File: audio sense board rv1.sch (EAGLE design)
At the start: 33 parts, among them IC2 TSOP38238, J1 PJRAN1X1U01X, J2 PJRAN1X1U01X, Q1 2N3904, Q2 2N3904

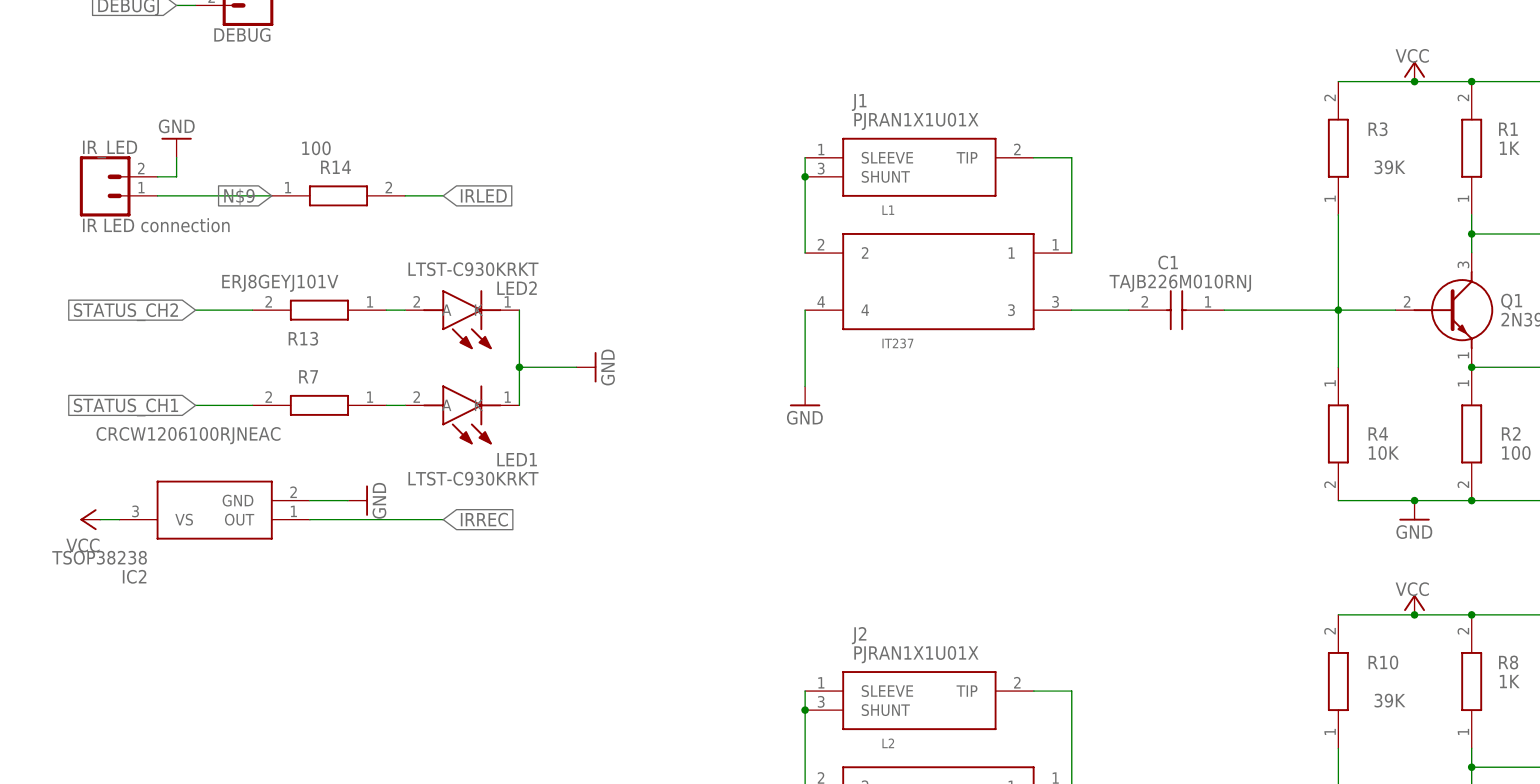
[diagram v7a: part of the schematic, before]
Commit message: update component values on output LEDs
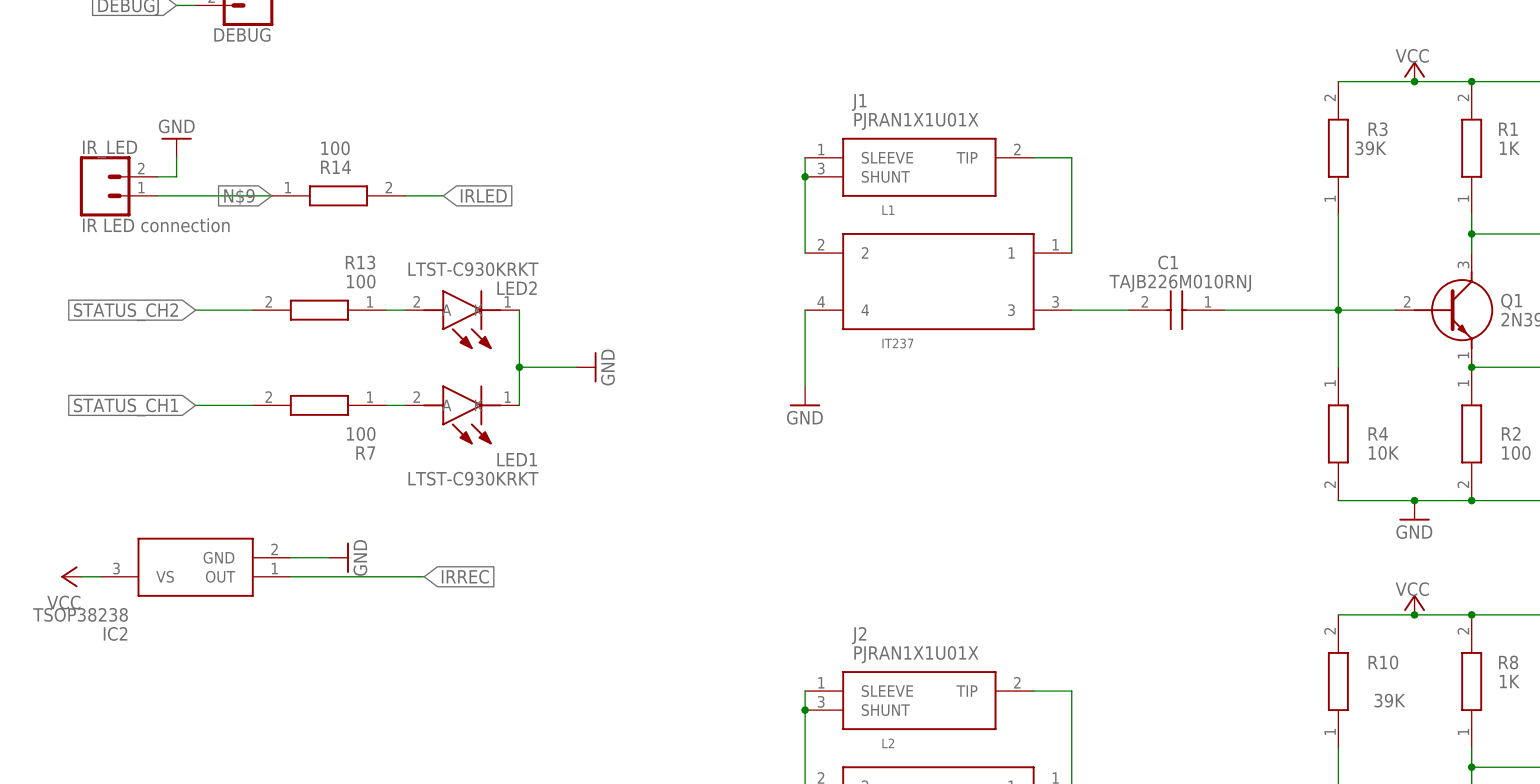
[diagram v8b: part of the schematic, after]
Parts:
- R13: value ERJ8GEYJ101V -> 100
- R7: value CRCW1206100RJNEAC -> 100; device Samac Populated:CRCW1206100RJNEAC -> Samac Populated:ERJ8GEYJ101V
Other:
- moved on the sheet: IC2
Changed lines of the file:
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@@
 <part name="LED1" library="Samac Populated" deviceset="LTST-C930KRKT" device=""/>
 <part name="LED2" library="Samac Populated" deviceset="LTST-C930KRKT" device=""/>
-<part name="R7" library="Samac Populated" deviceset="CRCW1206100RJNEAC" device=""/>
-<part name="R13" library="Samac Populated" deviceset="ERJ8GEYJ101V" device=""/>
+<part name="R7" library="Samac Populated" deviceset="ERJ8GEYJ101V" device="" value="100"/>
+<part name="R13" library="Samac Populated" deviceset="ERJ8GEYJ101V" device="" value="100"/>
 <part name="GND4" library="supply1" library_urn="urn:adsk.eagle:library:371" deviceset="GND" device=""/>
 <part name="R14" library="Samac Populated" deviceset="CRCW1206100RJNEAC" device="" value="100"/>
@@
 <attribute name="VALUE" x="-17.78" y="137.16" size="1.778" layer="96" rot="R90"/>
 </instance>
-<instance part="IC2" gate="G$1" x="-137.16" y="30.48" smashed="yes" rot="R180">
-<attribute name="NAME" x="-158.75" y="22.86" size="1.778" layer="95" rot="R180" align="center-left"/>
-<attribute name="VALUE" x="-158.75" y="25.4" size="1.778" layer="96" rot="R180" align="center-left"/>
+<instance part="IC2" gate="G$1" x="-139.7" y="22.86" smashed="yes" rot="R180">
+<attribute name="NAME" x="-161.29" y="15.24" size="1.778" layer="95" rot="R180" align="center-left"/>
+<attribute name="VALUE" x="-161.29" y="17.78" size="1.778" layer="96" rot="R180" align="center-left"/>
 </instance>
 <instance part="GND5" gate="1" x="-154.94" y="81.28" smashed="yes" rot="R180">
@@
 <attribute name="NAME" x="-167.64" y="79.248" size="1.778" layer="95" font="vector"/>
 </instance>
-<instance part="GND6" gate="1" x="-129.54" y="33.02" smashed="yes" rot="R90">
-<attribute name="VALUE" x="-127" y="30.48" size="1.778" layer="96" rot="R90"/>
+<instance part="GND6" gate="1" x="-132.08" y="25.4" smashed="yes" rot="R90">
+<attribute name="VALUE" x="-129.54" y="22.86" size="1.778" layer="96" rot="R90"/>
 </instance>
 <instance part="P+1" gate="VCC" x="-25.4" y="134.62" smashed="yes" rot="R270">
 <attribute name="VALUE" x="-27.94" y="137.16" size="1.778" layer="96"/>
 </instance>
-<instance part="P+2" gate="VCC" x="-167.64" y="30.48" smashed="yes" rot="R90">
-<attribute name="VALUE" x="-165.1" y="27.94" size="1.778" layer="96" rot="R180"/>
+<instance part="P+2" gate="VCC" x="-170.18" y="22.86" smashed="yes" rot="R90">
+<attribute name="VALUE" x="-167.64" y="20.32" size="1.778" layer="96" rot="R180"/>
 </instance>
 <instance part="GND7" gate="1" x="-73.66" y="134.62" smashed="yes" rot="R270">
@@
 </instance>
 <instance part="R7" gate="G$1" x="-127" y="45.72" smashed="yes" rot="R180">
-<attribute name="NAME" x="-135.89" y="49.53" size="1.778" layer="95" rot="R180" align="center-left"/>
-<attribute name="VALUE" x="-140.97" y="41.91" size="1.778" layer="96" rot="R180" align="center-left"/>
+<attribute name="NAME" x="-128.27" y="39.37" size="1.778" layer="95" rot="R180" align="center-left"/>
+<attribute name="VALUE" x="-128.27" y="41.91" size="1.778" layer="96" rot="R180" align="center-left"/>
 </instance>
 <instance part="R13" gate="G$1" x="-127" y="58.42" smashed="yes" rot="R180">
-<attribute name="NAME" x="-135.89" y="54.61" size="1.778" layer="95" rot="R180" align="center-left"/>
-<attribute name="VALUE" x="-133.35" y="62.23" size="1.778" layer="96" rot="R180" align="center-left"/>
+<attribute name="NAME" x="-128.27" y="64.77" size="1.778" layer="95" rot="R180" align="center-left"/>
+<attribute name="VALUE" x="-128.27" y="62.23" size="1.778" layer="96" rot="R180" align="center-left"/>
 </instance>
 <instance part="GND4" gate="1" x="-99.06" y="50.8" smashed="yes" rot="R90">
@@
 <instance part="R14" gate="G$1" x="-142.24" y="73.66" smashed="yes">
 <attribute name="NAME" x="-135.89" y="77.47" size="1.778" layer="95" align="center-left"/>
-<attribute name="VALUE" x="-138.43" y="80.01" size="1.778" layer="96" align="center-left"/>
+<attribute name="VALUE" x="-135.89" y="80.01" size="1.778" layer="96" align="center-left"/>
 </instance>
 <instance part="J1" gate="G$1" x="-71.12" y="78.74" smashed="yes">
@@
 <instance part="R3" gate="G$1" x="0" y="71.12" smashed="yes" rot="R90">
 <attribute name="NAME" x="3.81" y="82.55" size="1.778" layer="95" align="center-left"/>
-<attribute name="VALUE" x="8.89" y="77.47" size="1.778" layer="96" rot="R180" align="center-left"/>
+<attribute name="VALUE" x="6.35" y="80.01" size="1.778" layer="96" rot="R180" align="center-left"/>
 </instance>
 <instance part="R4" gate="G$1" x="0" y="50.8" smashed="yes" rot="R270">
@@
 <pinref part="GND6" gate="1" pin="GND"/>
 <pinref part="IC2" gate="G$1" pin="GND"/>
-<wire x1="-132.08" y1="33.02" x2="-137.16" y2="33.02" width="0.1524" layer="91"/>
+<wire x1="-134.62" y1="25.4" x2="-139.7" y2="25.4" width="0.1524" layer="91"/>
 </segment>
 <segment>
@@
 <pinref part="P+2" gate="VCC" pin="VCC"/>
 <pinref part="IC2" gate="G$1" pin="VS"/>
-<wire x1="-162.56" y1="30.48" x2="-165.1" y2="30.48" width="0.1524" layer="91"/>
+<wire x1="-165.1" y1="22.86" x2="-167.64" y2="22.86" width="0.1524" layer="91"/>
 </segment>
 <segment>
@@
 <segment>
 <pinref part="IC2" gate="G$1" pin="OUT"/>
-<wire x1="-137.16" y1="30.48" x2="-119.38" y2="30.48" width="0.1524" layer="91"/>
-<label x="-119.38" y="30.48" size="1.778" layer="95" xref="yes"/>
-</segment>
-<segment>
+<wire x1="-139.7" y1="22.86" x2="-121.92" y2="22.86" width="0.1524" layer="91"/>
+<label x="-121.92" y="22.86" size="1.778" layer="95" xref="yes"/>
+</segment>
+<segment>
